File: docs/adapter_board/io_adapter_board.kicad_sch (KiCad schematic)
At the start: 9 parts, among them J1 Fan Signal, J2 To ESP32 board, Q1 2N2222, U1 EL817

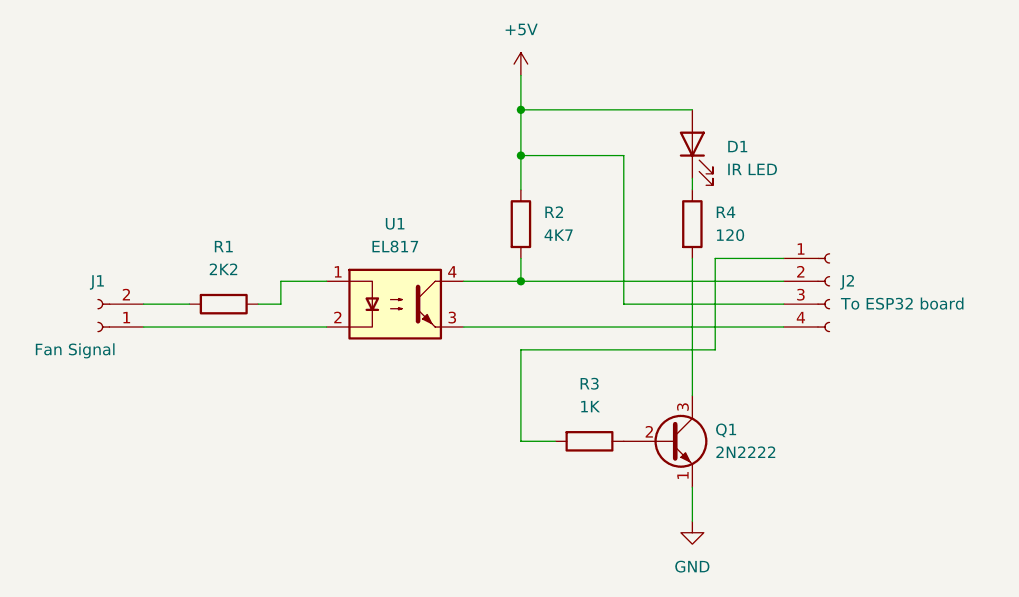
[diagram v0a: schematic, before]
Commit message: Added schematics and pictures regarding the adaptation for the Delba heater.
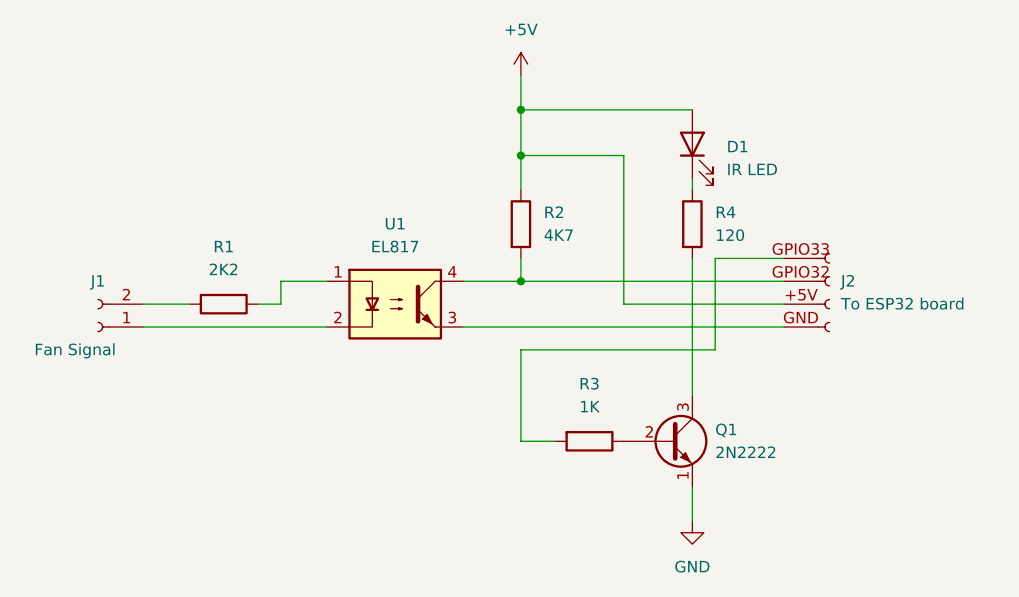
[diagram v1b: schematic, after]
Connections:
- net +5V: now also J2.+5V (Pin_3); no longer J2.3 (Pin_3)
- net at U1.3: now also J2.GND (Pin_4); no longer J2.4 (Pin_4)
- net at R2.2, U1.4: now also J2.GPIO32 (Pin_2); no longer J2.2 (Pin_2)
- net at R3.2: now also J2.GPIO33 (Pin_1); no longer J2.1 (Pin_1)
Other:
- moved on the sheet: J2
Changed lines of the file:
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@@
       (effects (font (size 1.27 1.27)) hide)
     )
-    (pin "1")
-    (pin "2")
-    (pin "3")
-    (pin "4")
+    (pin "GPIO33")
+    (pin "GPIO32")
+    (pin "+5V")
+    (pin "GND")
   )
   (symbol (lib_id "Device:LED") (at 170.18 81.28 90) (unit 1)

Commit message: Documentation fix
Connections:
- net GND: now also J2.GND (Pin_4), U1.3
- net +5V renamed +3V3
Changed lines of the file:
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@@
   (junction (at 151.13 82.55) (diameter 0) (color 0 0 0 0)
   )
+  (junction (at 176.53 101.6) (diameter 0) (color 0 0 0 0)
+  )
   (junction (at 151.13 77.47) (diameter 0) (color 0 0 0 0)
   )
@@
     (stroke (width 0) (type default) (color 0 0 0 0))
   )
+  (wire (pts (xy 176.53 101.6) (xy 180.34 101.6))
+    (stroke (width 0) (type default) (color 0 0 0 0))
+  )
   (wire (pts (xy 151.13 77.47) (xy 151.13 82.55))
     (stroke (width 0) (type default) (color 0 0 0 0))
   )
-  (wire (pts (xy 144.78 101.6) (xy 180.34 101.6))
+  (wire (pts (xy 144.78 101.6) (xy 176.53 101.6))
+    (stroke (width 0) (type default) (color 0 0 0 0))
+  )
+  (wire (pts (xy 176.53 101.6) (xy 176.53 104.14))
     (stroke (width 0) (type default) (color 0 0 0 0))
   )
@@
       (effects (font (size 1.27 1.27)) hide)
     )
-    (pin "GPIO33")
-    (pin "GPIO32")
     (pin "+5V")
     (pin "GND")
+    (pin "GPIO32")
+    (pin "GPIO33")
   )
   (symbol (lib_id "Device:LED") (at 170.18 81.28 90) (unit 1)
@@
     (pin "2")
   )
-  (symbol (lib_id "power:+5V") (at 151.13 73.66 0) (unit 1)
-    (in_bom yes) (on_board yes)
+  (symbol (lib_id "Device:R") (at 151.13 90.17 0) (unit 1)
+    (in_bom yes) (on_board yes) (fields_autoplaced)
+    (property "Reference" "R2" (id 0) (at 153.67 88.8999 0)
+      (effects (font (size 1.27 1.27)) (justify left))
+    )
+    (property "Value" "4K7" (id 1) (at 153.67 91.4399 0)
+      (effects (font (size 1.27 1.27)) (justify left))
+    )
+    (property "Footprint" "" (id 2) (at 149.352 90.17 90)
+      (effects (font (size 1.27 1.27)) hide)
+    )
+    (property "Datasheet" "~" (id 3) (at 151.13 90.17 0)
+      (effects (font (size 1.27 1.27)) hide)
+    )
+    (pin "1")
+    (pin "2")
+  )
+  (symbol (lib_id "power:GND") (at 176.53 104.14 0) (unit 1)
+    (in_bom yes) (on_board yes) (fields_autoplaced)
+    (property "Reference" "#PWR?" (id 0) (at 176.53 110.49 0)
+      (effects (font (size 1.27 1.27)) hide)
+    )
+    (property "Value" "GND" (id 1) (at 176.53 109.22 0))
+    (property "Footprint" "" (id 2) (at 176.53 104.14 0)
+      (effects (font (size 1.27 1.27)) hide)
+    )
+    (property "Datasheet" "" (id 3) (at 176.53 104.14 0)
+      (effects (font (size 1.27 1.27)) hide)
+    )
+    (pin "1")
+  )
+  (symbol (lib_id "power:+3.3V") (at 151.13 73.66 0) (unit 1)
+    (in_bom yes) (on_board yes) (fields_autoplaced)
     (property "Reference" "#PWR?" (id 0) (at 151.13 77.47 0)
       (effects (font (size 1.27 1.27)) hide)
     )
-    (property "Value" "+5V" (id 1) (at 151.13 68.58 0))
+    (property "Value" "+3.3V" (id 1) (at 151.13 68.58 0))
     (property "Footprint" "" (id 2) (at 151.13 73.66 0)
       (effects (font (size 1.27 1.27)) hide)
@@
     )
     (pin "1")
-  )
-  (symbol (lib_id "Device:R") (at 151.13 90.17 0) (unit 1)
-    (in_bom yes) (on_board yes) (fields_autoplaced)
-    (property "Reference" "R2" (id 0) (at 153.67 88.8999 0)
-      (effects (font (size 1.27 1.27)) (justify left))
-    )
-    (property "Value" "4K7" (id 1) (at 153.67 91.4399 0)
-      (effects (font (size 1.27 1.27)) (justify left))
-    )
-    (property "Footprint" "" (id 2) (at 149.352 90.17 90)
-      (effects (font (size 1.27 1.27)) hide)
-    )
-    (property "Datasheet" "~" (id 3) (at 151.13 90.17 0)
-      (effects (font (size 1.27 1.27)) hide)
-    )
-    (pin "1")
-    (pin "2")
   )
   (sheet_instances
@@
       (reference "#PWR?") (unit 1) (value "GND") (footprint "")
     )
-    (path "/a944fd4e-c59a-4ea7-a0a8-6be4330872de"
-      (reference "#PWR?") (unit 1) (value "+5V") (footprint "")
+    (path "/e63c64b6-caf4-4b0c-874d-4aa57ce0edfc"
+      (reference "#PWR?") (unit 1) (value "GND") (footprint "")
+    )
+    (path "/ff5ead9b-37b8-4bc9-9ac4-39775f57c6cf"
+      (reference "#PWR?") (unit 1) (value "+3.3V") (footprint "")
     )
     (path "/a620b9b1-d517-4b44-83c9-c24e92d7d43f"

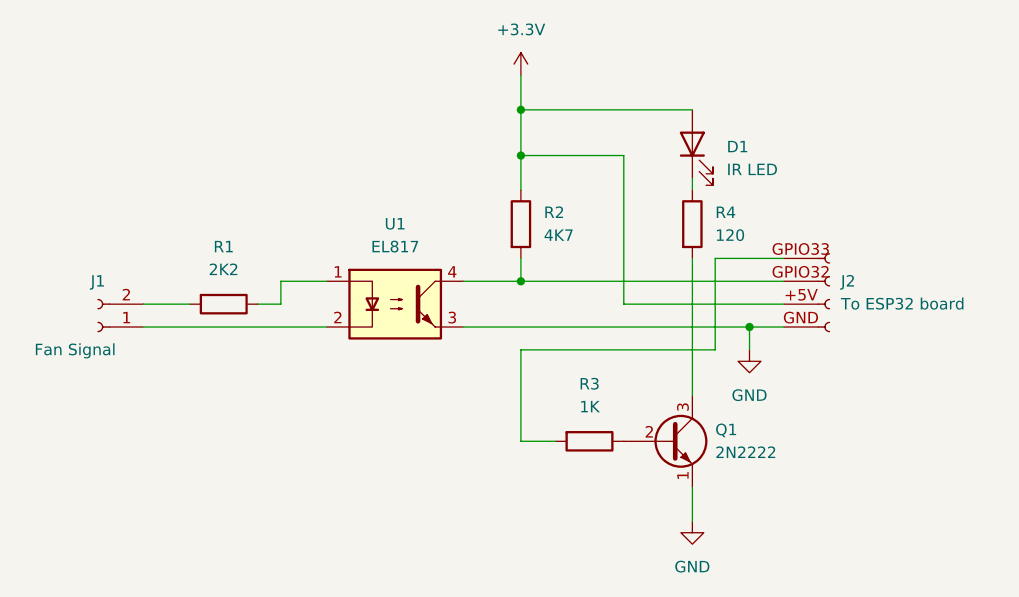
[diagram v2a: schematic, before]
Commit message: Schematic diagram fix
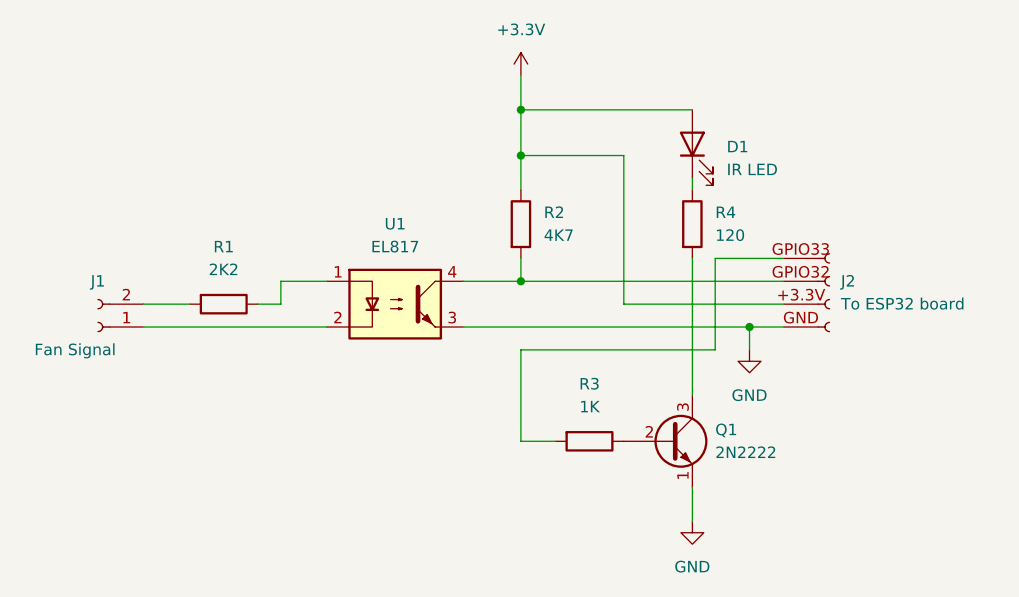
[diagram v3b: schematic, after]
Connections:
- net +3V3: now also J2.+3.3V (Pin_3); no longer J2.+5V (Pin_3)
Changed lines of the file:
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@@
       (effects (font (size 1.27 1.27)) hide)
     )
-    (pin "+5V")
+    (pin "+3.3V")
     (pin "GND")
     (pin "GPIO32")
